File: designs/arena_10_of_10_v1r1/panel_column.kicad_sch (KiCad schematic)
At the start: 3 parts

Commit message: Added initial annotation.
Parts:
- gave numbers to parts that had none: 3

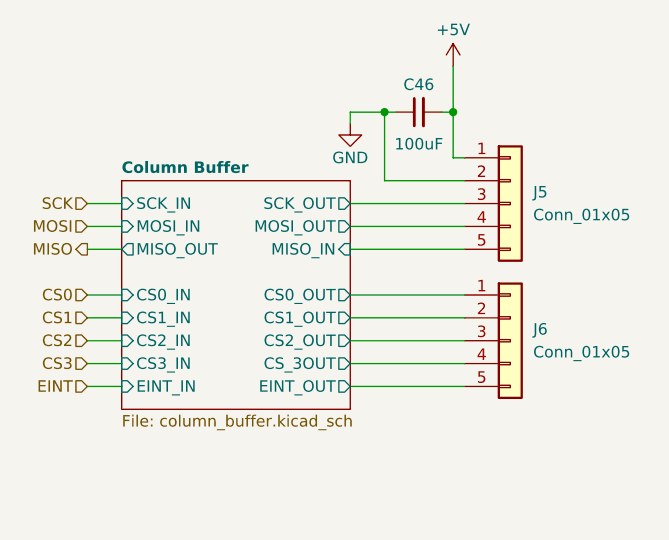
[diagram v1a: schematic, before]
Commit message: Finished footprint assignment.
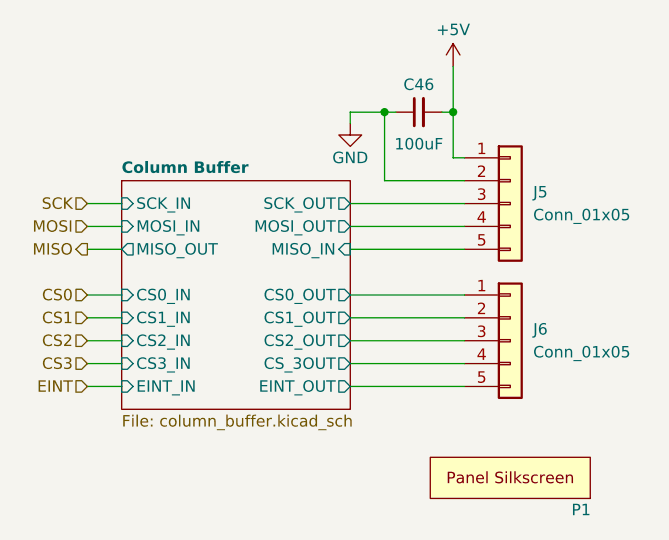
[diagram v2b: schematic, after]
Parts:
- added P1: NA, panel_silk:Panel_Silk, symbol panel_silk:panel_silk
- C46: footprint (none) -> Capacitor_SMD:C_1210_3225Metric
- J5, J6: footprint (none) -> Connector_PinHeader_2.54mm:PinHeader_1x05_P2.54mm_Vertical
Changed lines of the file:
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@@
 			)
 		)
-		(property "Footprint" ""
+		(property "Footprint" "Connector_PinHeader_2.54mm:PinHeader_1x05_P2.54mm_Vertical"
 			(at 161.29 69.85 0)
 			(effects
@@
 			)
 		)
-		(property "Footprint" ""
+		(property "Footprint" "Capacitor_SMD:C_1210_3225Metric"
 			(at 151.13 59.69 0)
 			(effects
@@
 				(path "/056666d2-2c8f-491c-bcad-db3c517779a8/3aea6610-f2a3-4b21-99b1-2866223bb12f/f30e8937-4e73-4e94-bb30-d8448d44cc0d"
 					(reference "C72")
+					(unit 1)
+				)
+			)
+		)
+	)
+	(symbol
+		(lib_id "panel_silk:panel_silk")
+		(at 161.29 100.33 180)
+		(unit 1)
+		(exclude_from_sim no)
+		(in_bom yes)
+		(on_board yes)
+		(dnp no)
+		(property "Reference" "P1"
+			(at 169.164 103.886 0)
+			(effects
+				(font
+					(size 1.27 1.27)
+				)
+			)
+		)
+		(property "Value" "NA"
+			(at 161.29 105.41 0)
+			(effects
+				(font
+					(size 1.27 1.27)
+				)
+				(hide yes)
+			)
+		)
+		(property "Footprint" "panel_silk:Panel_Silk"
+			(at 161.29 100.33 0)
+			(effects
+				(font
+					(size 1.27 1.27)
+				)
+				(hide yes)
+			)
+		)
+		(property "Datasheet" ""
+			(at 161.29 100.33 0)
+			(effects
+				(font
+					(size 1.27 1.27)
+				)
+				(hide yes)
+			)
+		)
+		(property "Description" ""
+			(at 161.29 100.33 0)
+			(effects
+				(font
+					(size 1.27 1.27)
+				)
+				(hide yes)
+			)
+		)
+		(instances
+			(project ""
+				(path "/056666d2-2c8f-491c-bcad-db3c517779a8/3aea6610-f2a3-4b21-99b1-2866223bb12f/2d48c774-5bc7-44a4-9df6-3d6978bb1a97"
+					(reference "P8")
+					(unit 1)
+				)
+				(path "/056666d2-2c8f-491c-bcad-db3c517779a8/3aea6610-f2a3-4b21-99b1-2866223bb12f/2ea8ae5a-de16-4e05-aa10-4b631d39866b"
+					(reference "P10")
+					(unit 1)
+				)
+				(path "/056666d2-2c8f-491c-bcad-db3c517779a8/3aea6610-f2a3-4b21-99b1-2866223bb12f/3f550e36-6b1c-4366-9cef-eaf43ff57ed4"
+					(reference "P1")
+					(unit 1)
+				)
+				(path "/056666d2-2c8f-491c-bcad-db3c517779a8/3aea6610-f2a3-4b21-99b1-2866223bb12f/51470252-73d0-4c49-9e01-600741a5432e"
+					(reference "P3")
+					(unit 1)
+				)
+				(path "/056666d2-2c8f-491c-bcad-db3c517779a8/3aea6610-f2a3-4b21-99b1-2866223bb12f/5b4b3792-1e39-479f-bd98-38e020ce3fcb"
+					(reference "P9")
+					(unit 1)
+				)
+				(path "/056666d2-2c8f-491c-bcad-db3c517779a8/3aea6610-f2a3-4b21-99b1-2866223bb12f/92c2be2f-8271-448b-8aa4-e4b8407efff6"
+					(reference "P6")
+					(unit 1)
+				)
+				(path "/056666d2-2c8f-491c-bcad-db3c517779a8/3aea6610-f2a3-4b21-99b1-2866223bb12f/dd831cd8-a815-4f96-a072-dbf69e6ca36d"
+					(reference "P2")
+					(unit 1)
+				)
+				(path "/056666d2-2c8f-491c-bcad-db3c517779a8/3aea6610-f2a3-4b21-99b1-2866223bb12f/e576223b-3974-48ef-8061-d66ec99be93c"
+					(reference "P5")
+					(unit 1)
+				)
+				(path "/056666d2-2c8f-491c-bcad-db3c517779a8/3aea6610-f2a3-4b21-99b1-2866223bb12f/e9282780-0e45-440c-a214-c0eb816f51cd"
+					(reference "P4")
+					(unit 1)
+				)
+				(path "/056666d2-2c8f-491c-bcad-db3c517779a8/3aea6610-f2a3-4b21-99b1-2866223bb12f/f30e8937-4e73-4e94-bb30-d8448d44cc0d"
+					(reference "P7")
 					(unit 1)
 				)
@@
 			)
 		)
-		(property "Footprint" ""
+		(property "Footprint" "Connector_PinHeader_2.54mm:PinHeader_1x05_P2.54mm_Vertical"
 			(at 161.29 85.09 0)
 			(effects

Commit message: Worked on automatic layout of panels + conditioning components.
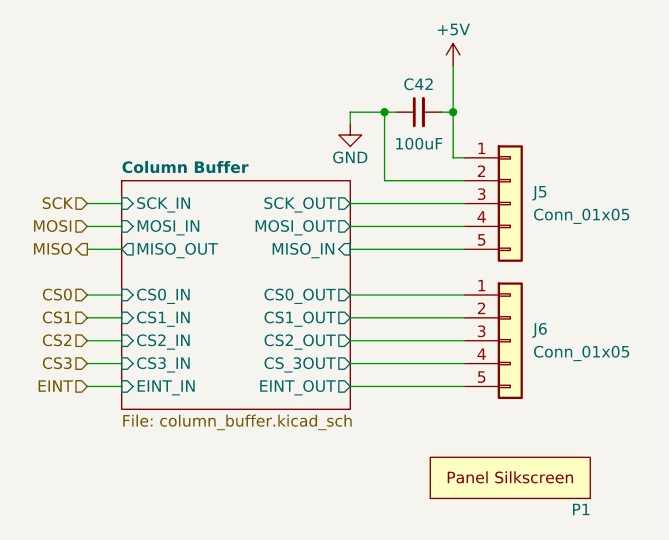
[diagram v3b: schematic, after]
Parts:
- renumbered C46 to C42
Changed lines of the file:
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@@
 		(on_board yes)
 		(dnp no)
-		(property "Reference" "C46"
+		(property "Reference" "C42"
 			(at 151.13 56.642 90)
 			(effects
@@
 				)
 				(path "/056666d2-2c8f-491c-bcad-db3c517779a8/3aea6610-f2a3-4b21-99b1-2866223bb12f/3f550e36-6b1c-4366-9cef-eaf43ff57ed4"
-					(reference "C46")
+					(reference "C42")
 					(unit 1)
 				)

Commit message: More work on layout. Fixed header issue.
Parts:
- J5, J6: footprint Connector_PinHeader_2.54mm:PinHeader_1x05_P2.54mm_Vertical -> Connector_PinSocket_2.54mm:PinSocket_1x05_P2.54mm_Vertical
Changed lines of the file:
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@@
 			)
 		)
-		(property "Footprint" "Connector_PinHeader_2.54mm:PinHeader_1x05_P2.54mm_Vertical"
+		(property "Footprint" "Connector_PinSocket_2.54mm:PinSocket_1x05_P2.54mm_Vertical"
 			(at 161.29 69.85 0)
 			(effects
@@
 			)
 		)
-		(property "Footprint" "Connector_PinHeader_2.54mm:PinHeader_1x05_P2.54mm_Vertical"
+		(property "Footprint" "Connector_PinSocket_2.54mm:PinSocket_1x05_P2.54mm_Vertical"
 			(at 161.29 85.09 0)
 			(effects
